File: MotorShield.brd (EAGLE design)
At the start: 85 x 56 mm, 88 parts, among them IC1 OPA4340E, IC2 OPA4340E

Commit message: marked gpios that are used by s.usv basic, see #10
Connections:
- new net N$16: PCB1.3
- new net N$19: PCB1.27
- new net N$20: PCB1.28
- new net N$21: PCB1.5
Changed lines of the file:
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@@
 <via x="34.29" y="40.64" extent="1-16" drill="0.35"/>
+</signal>
+<signal name="N$16">
+<contactref element="PCB1" pad="3"/>
+</signal>
+<signal name="N$19">
+<contactref element="PCB1" pad="27"/>
+</signal>
+<signal name="N$20">
+<contactref element="PCB1" pad="28"/>
+</signal>
+<signal name="N$21">
+<contactref element="PCB1" pad="5"/>
 </signal>
 </signals>

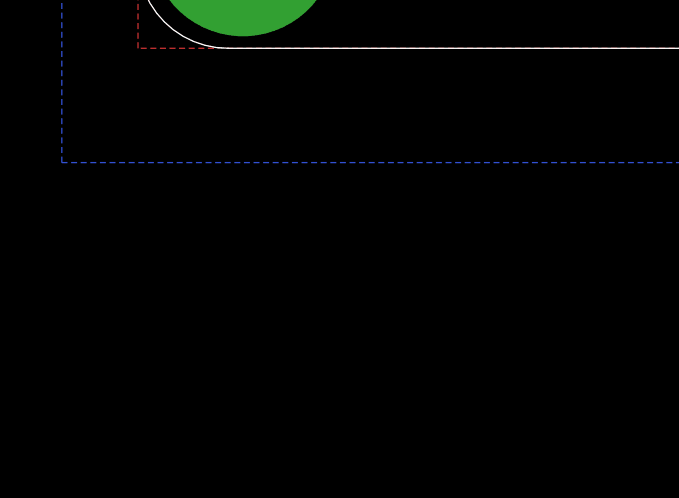
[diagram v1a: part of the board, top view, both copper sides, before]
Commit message: added 74HCT125D for DotStar pixels, see #3
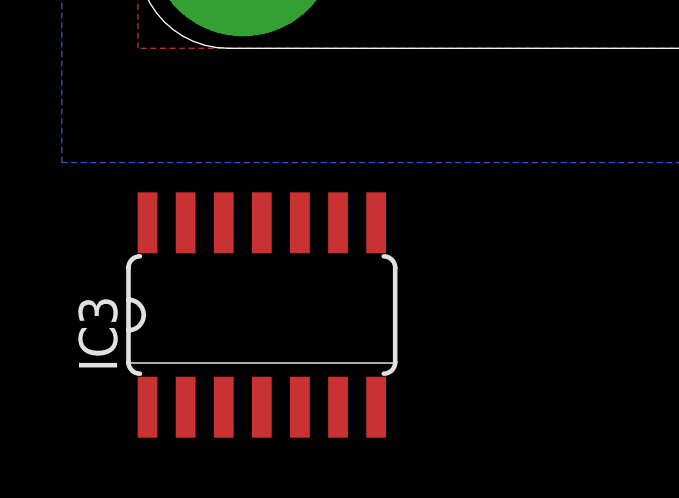
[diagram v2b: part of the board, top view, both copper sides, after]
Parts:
- added IC3: 74HCT125D, 74xx-eu:SO14
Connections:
- new net DOTCLK: IC3.3
- new net DOTDAT: IC3.6
- new net SPI0CE1: IC3.1, IC3.4, PCB1.26
- new net VCC: IC3.14
- net CLK: now also IC3.2
- net DIN: now also IC3.5
- net GND: now also IC3.10, IC3.12, IC3.13, IC3.7, IC3.9
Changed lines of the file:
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@@
 <attribute name="VALUE" x="76.835" y="6.985" size="1.27" layer="27" rot="R270"/>
 </element>
+<element name="IC3" library="74xx-eu" package="SO14" value="74HCT125D" x="4.1275" y="-8.89"/>
 </elements>
 <signals>
@@
 <wire x1="76.835" y1="3.175" x2="80.6" y2="3.175" width="2.54" layer="1"/>
 <wire x1="80.6" y1="3.175" x2="80.645" y2="3.13" width="2.54" layer="1"/>
+<contactref element="IC3" pad="7"/>
+<contactref element="IC3" pad="10"/>
+<contactref element="IC3" pad="12"/>
+<contactref element="IC3" pad="13"/>
+<contactref element="IC3" pad="9"/>
+<wire x1="2.8575" y1="-5.8166" x2="1.5875" y2="-5.8166" width="0" layer="19" extent="1-1"/>
+<wire x1="5.3975" y1="-5.8166" x2="2.8575" y2="-5.8166" width="0" layer="19" extent="1-1"/>
+<wire x1="6.6675" y1="-5.8166" x2="5.3975" y2="-5.8166" width="0" layer="19" extent="1-1"/>
+<wire x1="7.9375" y1="-11.9634" x2="6.6675" y2="-5.8166" width="0" layer="19" extent="1-1"/>
+<wire x1="2.54" y1="16.51" x2="1.5875" y2="-5.8166" width="0" layer="19" extent="1-1"/>
 </signal>
 <signal name="V1">
@@
 <wire x1="22.86" y1="49.53" x2="29.53" y2="49.53" width="0.254" layer="16"/>
 <wire x1="29.53" y1="49.53" x2="31.23" y2="51.23" width="0.254" layer="16"/>
+<contactref element="IC3" pad="5"/>
+<wire x1="5.3975" y1="-11.9634" x2="20.0025" y2="44.6659" width="0" layer="19" extent="1-16"/>
 </signal>
 <signal name="DOUT">
@@
 <wire x1="24.4475" y1="47.625" x2="32.705" y2="47.625" width="0.254" layer="16"/>
 <wire x1="32.705" y1="47.625" x2="36.31" y2="51.23" width="0.254" layer="16"/>
+<contactref element="IC3" pad="2"/>
+<wire x1="1.5875" y1="-11.9634" x2="22.5425" y2="44.6659" width="0" layer="19" extent="1-16"/>
 </signal>
 <signal name="N$6">
@@
 <contactref element="PCB1" pad="5"/>
 </signal>
+<signal name="VCC">
+<contactref element="IC3" pad="14"/>
+</signal>
+<signal name="DOTCLK">
+<contactref element="IC3" pad="3"/>
+</signal>
+<signal name="DOTDAT">
+<contactref element="IC3" pad="6"/>
+</signal>
+<signal name="SPI0CE1">
+<contactref element="PCB1" pad="26"/>
+<contactref element="IC3" pad="4"/>
+<contactref element="IC3" pad="1"/>
+<wire x1="4.1275" y1="-11.9634" x2="38.85" y2="53.77" width="0" layer="19" extent="1-1"/>
+<wire x1="0.3175" y1="-11.9634" x2="4.1275" y2="-11.9634" width="0" layer="19" extent="1-1"/>
+</signal>
 </signals>

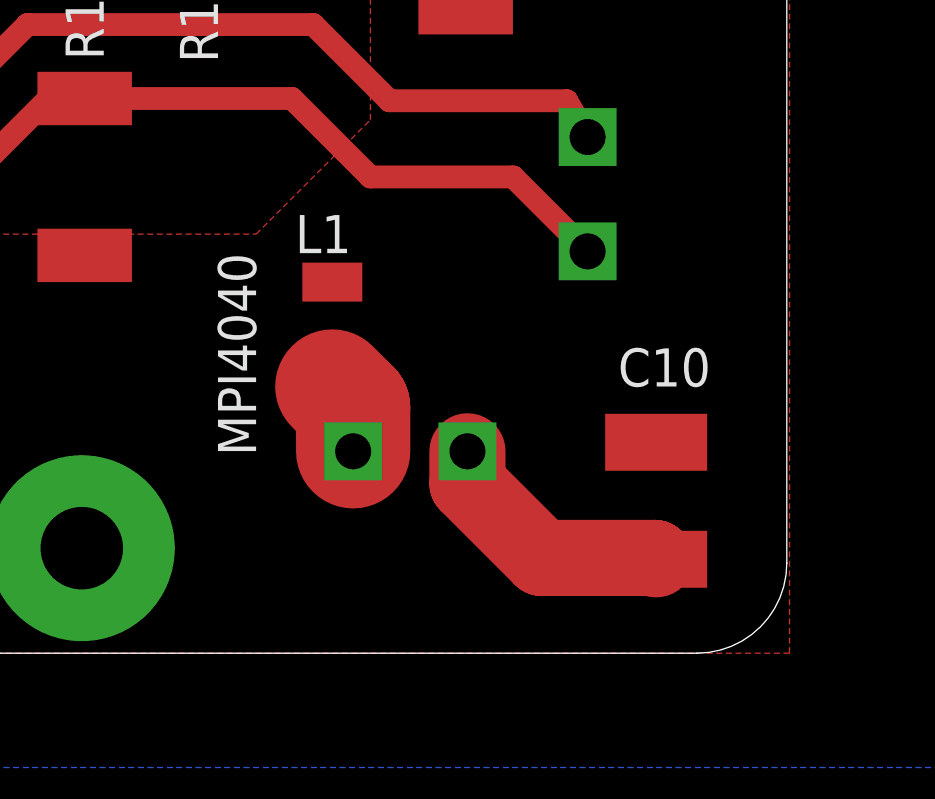
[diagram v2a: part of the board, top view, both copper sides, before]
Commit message: added label to power input closes #15
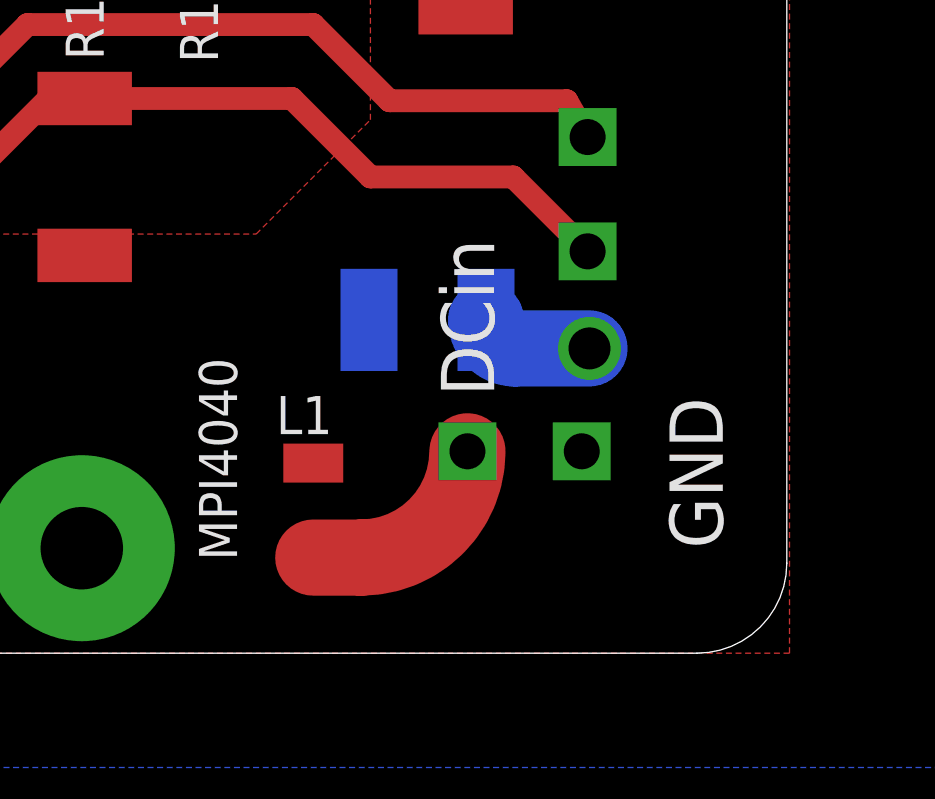
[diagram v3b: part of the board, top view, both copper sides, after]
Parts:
- moved C10 9.72 mm to (73.0, 11.1), flipped to the bottom, turned to 0 degrees
- moved L1 6.07 mm to (69.2, 4.76)
- moved U$16 3.81 mm to (71.8, -1.27)
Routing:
- net GND: track 55.5 -> 47.1 mm
- net 24V/8A: track 0.00 -> 3.84 mm, vias 0 -> 1
- net N$28: track 2.78 -> 6.61 mm
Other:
- board text added: "DCin"
- board text added: "GND"
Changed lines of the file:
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@@
 <setting verticaltext="up"/>
 </settings>
-<grid distance="0.0125" unitdist="inch" unit="inch" style="lines" multiple="1" display="yes" altdistance="0.00125" altunitdist="mil" altunit="mil"/>
+<grid distance="0.0125" unitdist="inch" unit="mm" style="lines" multiple="1" display="yes" altdistance="0.00125" altunitdist="mil" altunit="mil"/>
 <layers>
 <layer number="1" name="Top" color="4" fill="1" visible="yes" active="yes"/>
@@
 <board>
 <plain>
+<text x="82.8675" y="3.4925" size="1.778" layer="21" font="vector" ratio="16" rot="R90">GND</text>
+<text x="75.2475" y="8.5725" size="1.778" layer="21" font="vector" ratio="16" rot="R90">DCin</text>
 </plain>
 <attributes>
@@
 <attribute name="VALUE" x="25.0825" y="25.4" size="1.27" layer="28" rot="MR180"/>
 </element>
-<element name="U$16" library="Anschluss" package="AKL-BUCHSE" value="AKL-BUCHSE" x="67.945" y="-1.27" smashed="yes"/>
+<element name="U$16" library="Anschluss" package="AKL-BUCHSE" value="AKL-BUCHSE" x="71.755" y="-1.27" smashed="yes"/>
 <element name="U$34" library="Anschluss" package="AKL-BUCHSE" value="AKL-BUCHSE" x="10.16" y="-1.27" smashed="yes"/>
 <element name="U$58" library="MSC3008" package="SO16" value="MCP3008SO16" x="21.9075" y="41.5925" smashed="yes" rot="MR0">
@@
 <attribute name="VALUE" x="28.2575" y="47.3075" size="1.27" layer="28" rot="MR180"/>
 </element>
-<element name="L1" library="Spule" package="4040" value="MPI4040" x="69.85" y="10.795" smashed="yes" rot="R180">
-<attribute name="NAME" x="70.485" y="14.605" size="1.27" layer="21" rot="R180"/>
-<attribute name="VALUE" x="66.04" y="13.335" size="1.27" layer="21" rot="R270"/>
+<element name="L1" library="Spule" package="4040" value="MPI4040" x="69.215" y="4.7625" smashed="yes" rot="R180">
+<attribute name="NAME" x="69.85" y="8.5725" size="1.27" layer="21" rot="R180"/>
+<attribute name="VALUE" x="65.405" y="9.8425" size="1.27" layer="21" rot="R270"/>
 </element>
 <element name="U$1" library="Anschluss" package="AKL-BUCHSE" value="AKL-BUCHSE" x="21.59" y="-1.27" smashed="yes"/>
@@
 <element name="F7" library="SMD-Fuse" package="1812L050" value="POLY-FUSE" x="74.295" y="35.56" smashed="yes" rot="R270"/>
 <element name="F8" library="SMD-Fuse" package="1812L050" value="POLY-FUSE" x="74.295" y="48.26" smashed="yes" rot="R270"/>
-<element name="C10" library="rcl@1" package="C1812" value="" x="80.645" y="5.08" smashed="yes" rot="R270">
-<attribute name="NAME" x="79.375" y="8.89" size="1.27" layer="25"/>
-<attribute name="VALUE" x="76.835" y="6.985" size="1.27" layer="27" rot="R270"/>
+<element name="C10" library="rcl@1" package="C1812" value="" x="73.025" y="11.1125" smashed="yes" rot="MR0">
+<attribute name="NAME" x="76.835" y="9.8425" size="1.27" layer="26" rot="MR90"/>
+<attribute name="VALUE" x="74.93" y="7.3025" size="1.27" layer="28" rot="MR0"/>
 </element>
 <element name="IC3" library="74xx-eu" package="SO14" value="74HCT125D" x="4.1275" y="-8.89"/>
@@
 <wire x1="35.56" y1="19.05" x2="37.15" y2="19.05" width="0.762" layer="1"/>
 <via x="35.56" y="19.05" extent="1-16" drill="0.35"/>
-<polygon width="0.254" layer="16" isolate="0.254">
+<polygon width="0.254" layer="16" isolate="0.4064">
 <vertex x="-2.54" y="58.42"/>
 <vertex x="95.25" y="58.42"/>
@@
 <contactref element="PCB1" pad="20"/>
 <contactref element="PCB1" pad="25"/>
-<wire x1="74.355" y1="6.73" x2="74.355" y2="5.655" width="2.54" layer="1"/>
-<wire x1="74.355" y1="5.655" x2="76.835" y2="3.175" width="2.54" layer="1"/>
-<wire x1="76.835" y1="3.175" x2="80.6" y2="3.175" width="2.54" layer="1"/>
-<wire x1="80.6" y1="3.175" x2="80.645" y2="3.13" width="2.54" layer="1"/>
 <contactref element="IC3" pad="7"/>
 <contactref element="IC3" pad="10"/>
@@
 <contactref element="IC3" pad="13"/>
 <contactref element="IC3" pad="9"/>
+<wire x1="52.07" y1="39.37" x2="49.213" y2="38.4975" width="0" layer="19" extent="1-16"/>
+<wire x1="21.9875" y1="28.257" x2="19.37" y2="25.4" width="0" layer="19" extent="1-16"/>
+<wire x1="1.5875" y1="-5.8166" x2="2.54" y2="16.51" width="0" layer="19" extent="1-1"/>
 <wire x1="2.8575" y1="-5.8166" x2="1.5875" y2="-5.8166" width="0" layer="19" extent="1-1"/>
 <wire x1="5.3975" y1="-5.8166" x2="2.8575" y2="-5.8166" width="0" layer="19" extent="1-1"/>
 <wire x1="6.6675" y1="-5.8166" x2="5.3975" y2="-5.8166" width="0" layer="19" extent="1-1"/>
 <wire x1="7.9375" y1="-11.9634" x2="6.6675" y2="-5.8166" width="0" layer="19" extent="1-1"/>
-<wire x1="2.54" y1="16.51" x2="1.5875" y2="-5.8166" width="0" layer="19" extent="1-1"/>
 </signal>
 <signal name="V1">
@@
 <contactref element="L1" pad="P$1"/>
 <contactref element="U$16" pad="PLUS"/>
-<wire x1="70.545" y1="6.73" x2="70.545" y2="8.195" width="3.81" layer="1"/>
-<wire x1="70.545" y1="8.195" x2="69.85" y2="8.89" width="3.81" layer="1"/>
-<wire x1="69.85" y1="8.89" x2="69.85" y2="9.22" width="1.27" layer="1"/>
+<wire x1="74.355" y1="6.73" x2="70.8125" y2="3.1875" width="2.54" layer="1" curve="-90"/>
+<wire x1="70.8125" y1="3.1875" x2="69.215" y2="3.1875" width="2.54" layer="1"/>
 </signal>
 <signal name="24V/8A">
@@
 <vertex x="0" y="0"/>
 </polygon>
+<wire x1="74.975" y1="11.1125" x2="75.9275" y2="10.16" width="2.54" layer="16" curve="90"/>
+<wire x1="75.9275" y1="10.16" x2="78.4225" y2="10.16" width="2.54" layer="16"/>
+<via x="78.4225" y="10.16" extent="1-16" drill="1.4" shape="square"/>
 </signal>
 <signal name="N$4">

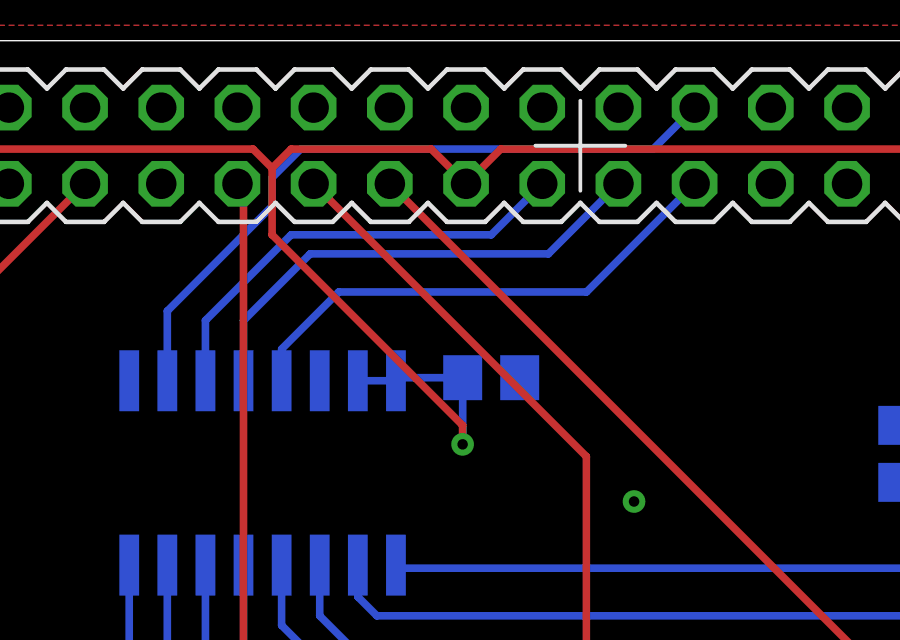
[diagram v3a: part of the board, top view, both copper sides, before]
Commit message: pump no. 5 is now controlled by GPIO23 fixes #10
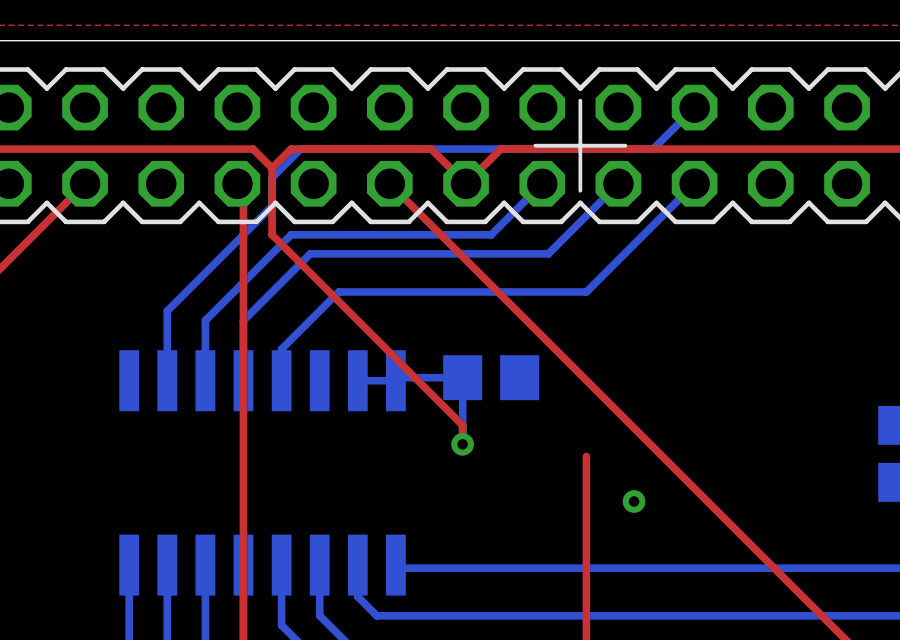
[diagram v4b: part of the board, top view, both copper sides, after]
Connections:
- net CS renamed CS_ADC
- new net CS_DOTSTARS: PCB1.26
- new net GPIO27: PCB1.13
- net M5: now also PCB1.16; no longer PCB1.13
- net SPI0CE1: no longer PCB1.26
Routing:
- net M5: track 33.7 -> 20.8 mm
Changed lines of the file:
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@@
 <wire x1="32.7" y1="21.3766" x2="32.7" y2="25.4" width="0.762" layer="1"/>
 <wire x1="32.7" y1="21.3766" x2="32.7406" y2="21.336" width="0.762" layer="1"/>
-<contactref element="PCB1" pad="13"/>
 <wire x1="32.7" y1="25.4" x2="32.7" y2="42.14" width="0.254" layer="1"/>
-<wire x1="32.7" y1="42.14" x2="23.61" y2="51.23" width="0.254" layer="1"/>
+<contactref element="PCB1" pad="16"/>
+<wire x1="32.7" y1="42.14" x2="26.15" y2="53.77" width="0" layer="19" extent="1-1"/>
 </signal>
 <signal name="M6">
@@
 <wire x1="18.7325" y1="27.305" x2="18.7325" y2="38.5191" width="0.254" layer="16"/>
 </signal>
-<signal name="CS">
+<signal name="CS_ADC">
 <contactref element="U$58" pad="10"/>
 <contactref element="PCB1" pad="24"/>
@@
 </signal>
 <signal name="SPI0CE1">
-<contactref element="PCB1" pad="26"/>
 <contactref element="IC3" pad="4"/>
 <contactref element="IC3" pad="1"/>
-<wire x1="4.1275" y1="-11.9634" x2="38.85" y2="53.77" width="0" layer="19" extent="1-1"/>
-<wire x1="0.3175" y1="-11.9634" x2="4.1275" y2="-11.9634" width="0" layer="19" extent="1-1"/>
+<wire x1="4.1275" y1="-11.9634" x2="0.3175" y2="-11.9634" width="0" layer="19" extent="1-1"/>
+</signal>
+<signal name="CS_DOTSTARS">
+<contactref element="PCB1" pad="26"/>
+</signal>
+<signal name="GPIO27">
+<contactref element="PCB1" pad="13"/>
 </signal>
 </signals>
